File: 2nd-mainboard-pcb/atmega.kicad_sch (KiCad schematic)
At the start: 22 parts, among them J2 Fan_12/5V_Regelung, J3 FAN0, J4 FAN1, J5 FAN2, J6 FAN3, U10 ATmega328PB-A, U7 TPM16050-S6TR, U8 RJK0456DPB-00-J5, U9 RJK0456DPB-00-J5, Y1 ECS-160-18-4X-CKM

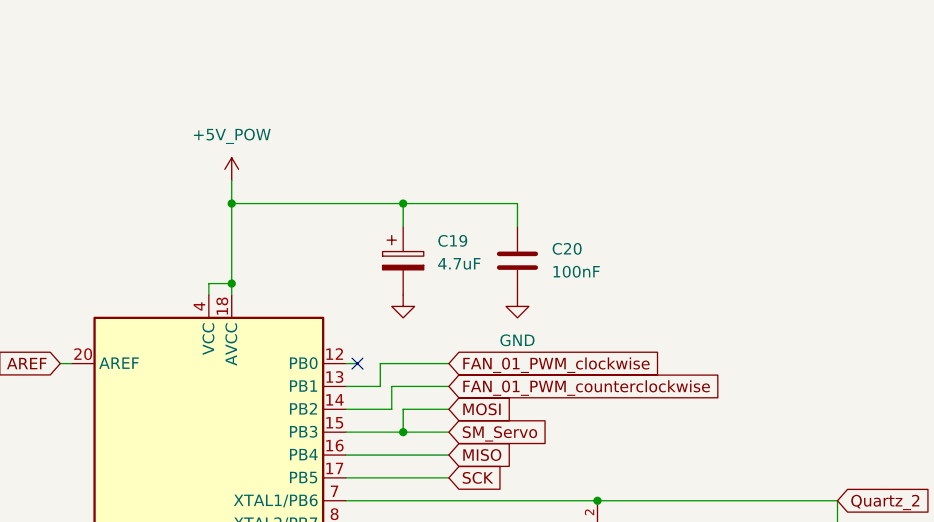
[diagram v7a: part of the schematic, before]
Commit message: DRC fehler behoben ca 200 stueck, jetzt gehts ans pcb ausschneiden
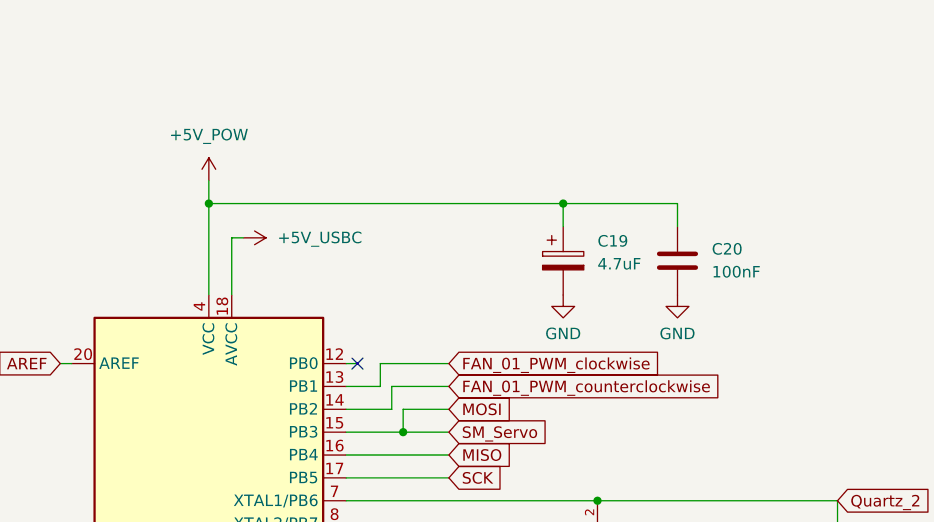
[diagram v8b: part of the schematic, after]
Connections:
- net +5V_POW: no longer U10.18 (AVCC)
- new net +5V_USBC: U10.18 (AVCC)
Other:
- moved on the sheet: C19, C20
